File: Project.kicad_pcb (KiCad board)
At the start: 2 copper layers, 26 parts, among them J1 USB_B, J2 Conn_01x02, J3 Conn_01x04, J4 Conn_01x04, K4 G3MB-202PDC5, Q4 2SC1815, SW1 SW_DIP_x01, U1 ESP-12E

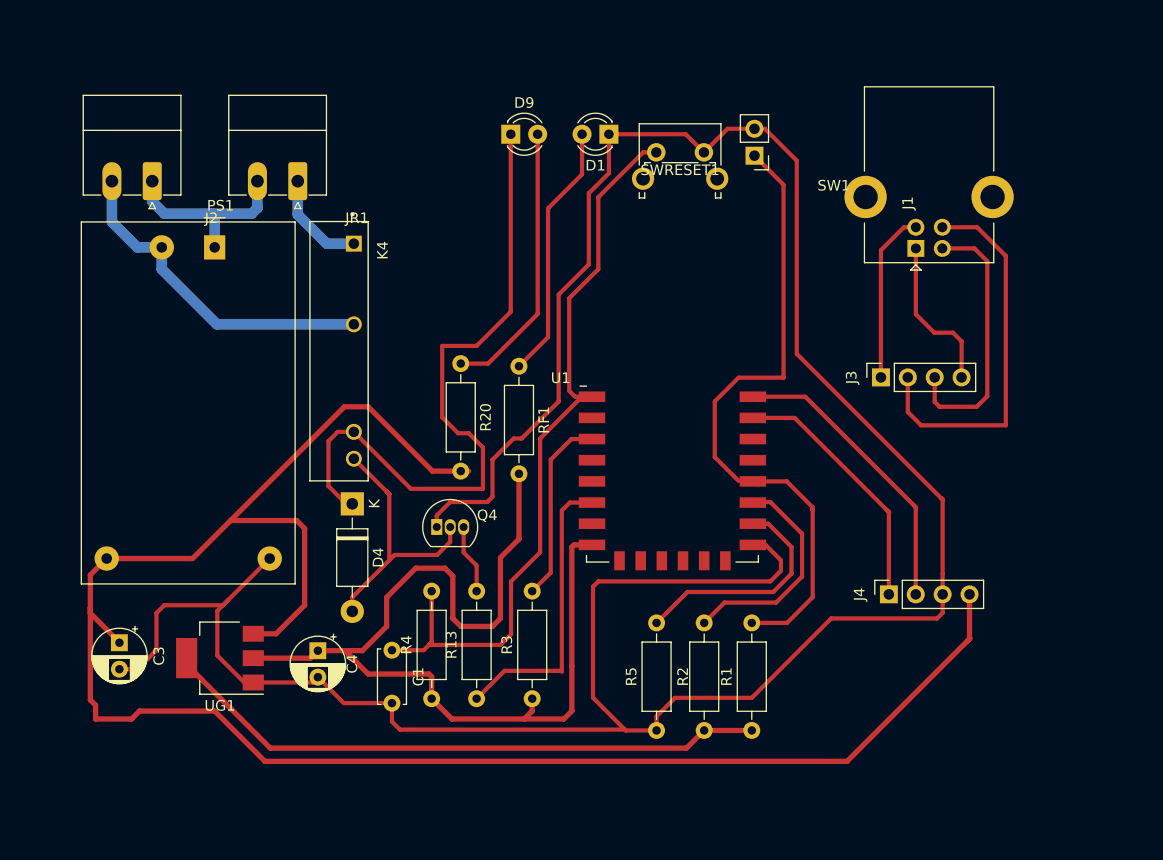
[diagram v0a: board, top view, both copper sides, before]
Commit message: Add new modifier
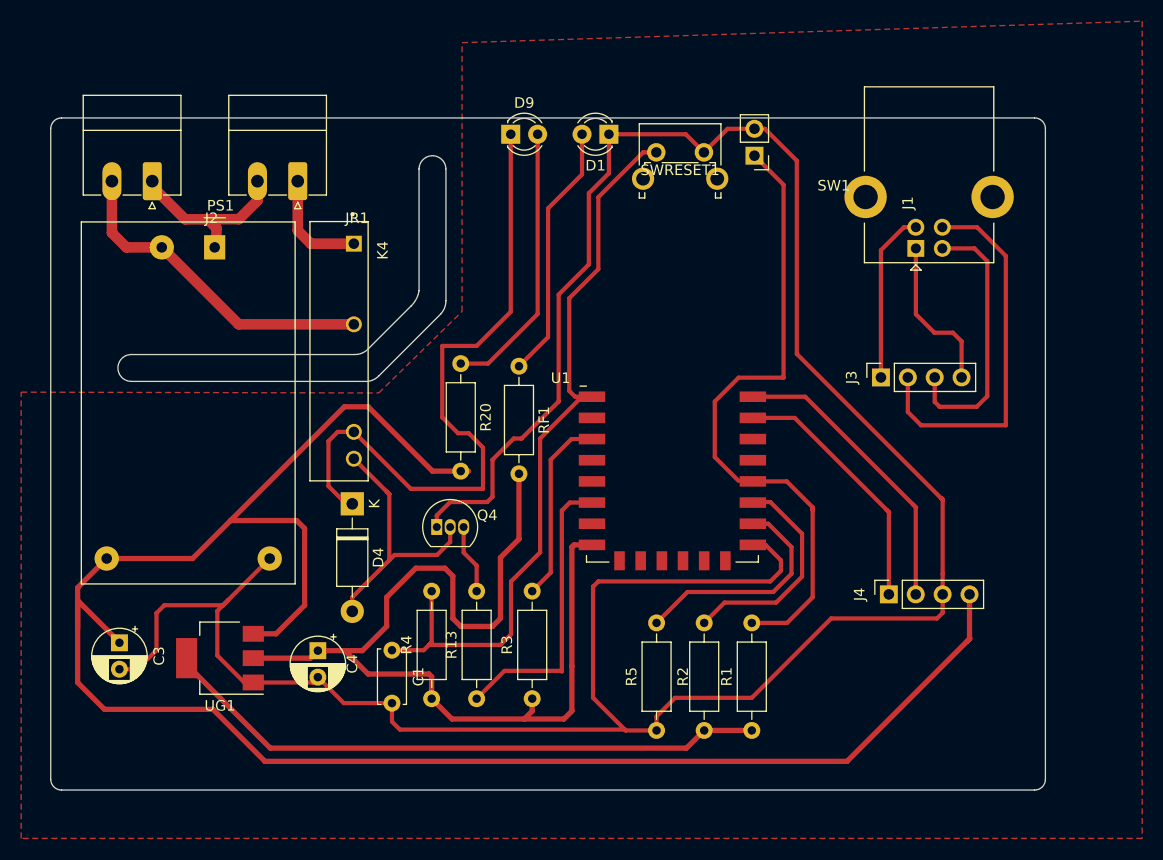
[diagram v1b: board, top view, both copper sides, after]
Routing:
- net +5V: track 178.0 -> 181.0 mm
- net /N: track 18.7 -> 17.3 mm
- net /12: track 9.86 -> 10.5 mm
- net /L: track 31.9 -> 31.3 mm
- added copper zone on F.Cu, net GND
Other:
- board outline added: 94 x 63.5 mm
